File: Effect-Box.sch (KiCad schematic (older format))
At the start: 0 parts

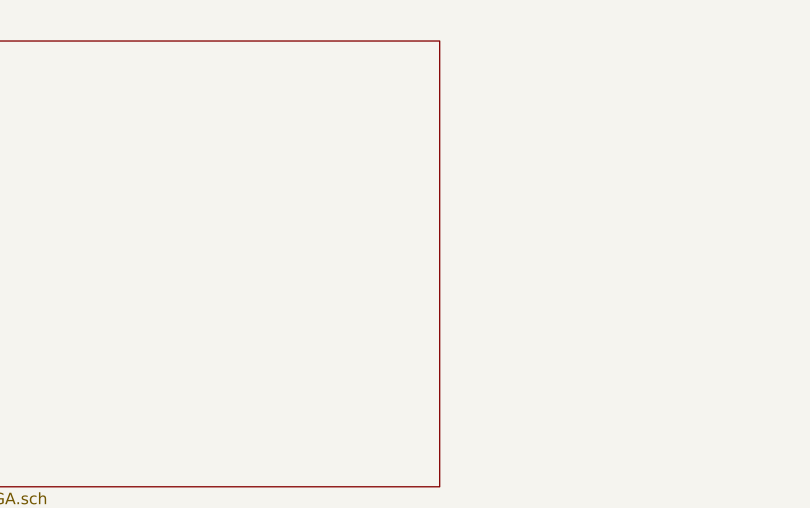
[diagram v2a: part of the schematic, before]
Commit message: Prepare FPGA I/O pins
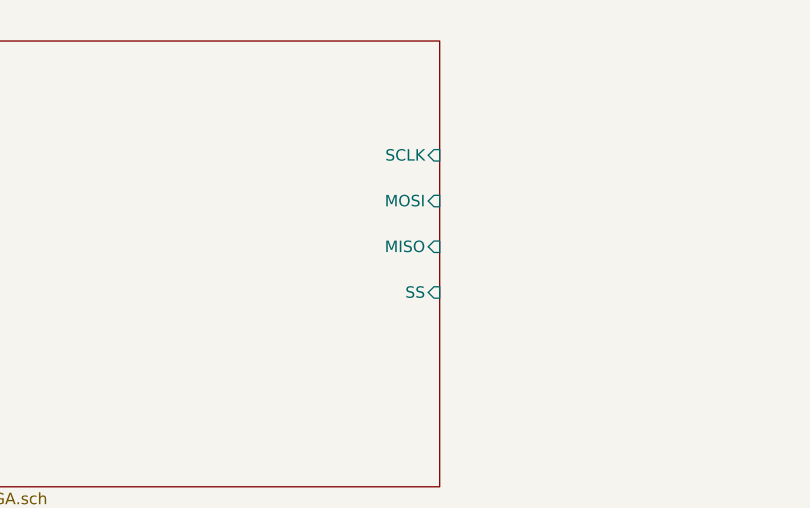
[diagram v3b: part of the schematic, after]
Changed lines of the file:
@@
 F0 "FPGA" 50
 F1 "FPGA.sch" 50
+F2 "SCLK" I R 3700 1900 50
+F3 "MOSI" I R 3700 2100 50
+F4 "MISO" I R 3700 2300 50
+F5 "SS" I R 3700 2500 50
 $EndSheet
 $Sheet

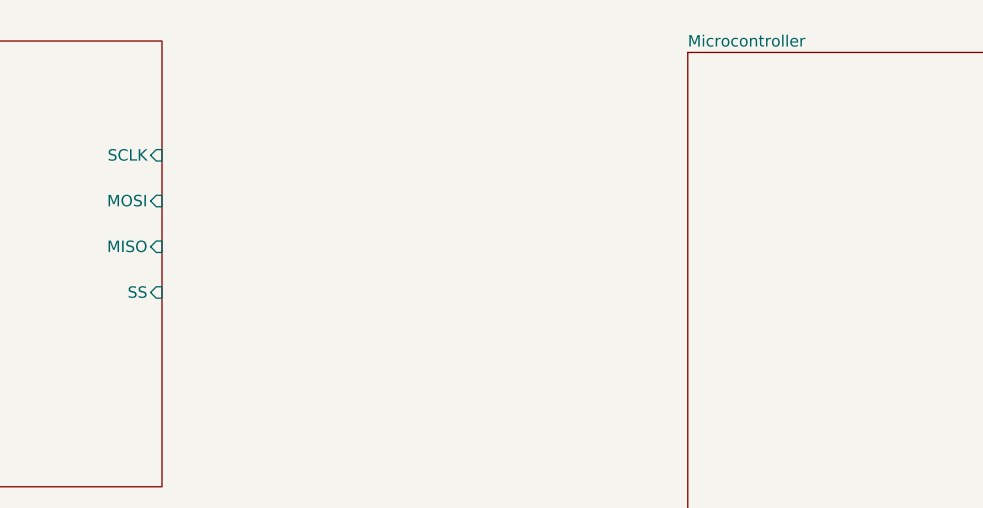
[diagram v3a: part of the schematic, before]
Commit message: Connect MCU to FPGA
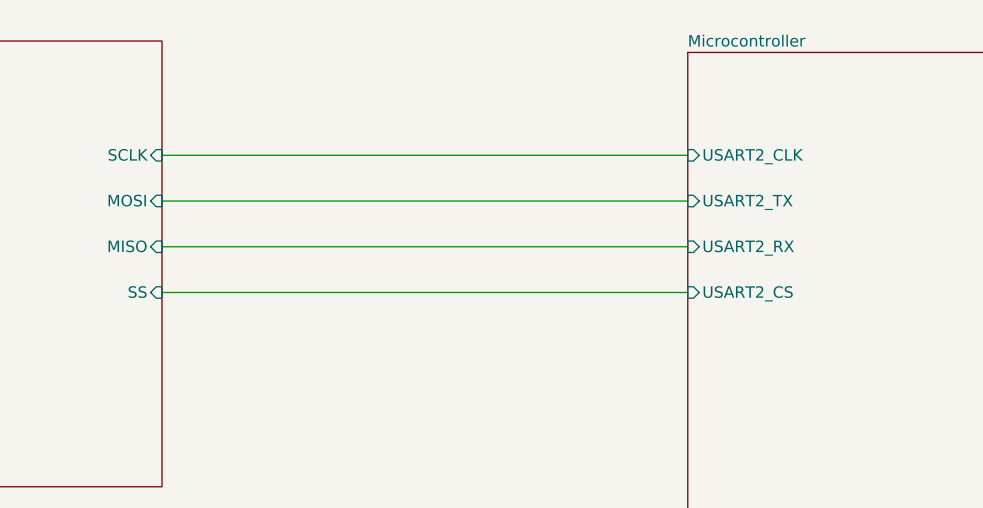
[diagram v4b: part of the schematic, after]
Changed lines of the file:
@@
 F0 "Microcontroller" 50
 F1 "microcontroller.sch" 50
+F2 "USART2_TX" I L 6000 2100 50
+F3 "USART2_RX" I L 6000 2300 50
+F4 "USART2_CLK" I L 6000 1900 50
+F5 "USART2_CS" I L 6000 2500 50
 $EndSheet
 $Sheet
@@
 F1 "power.sch" 50
 $EndSheet
+Wire Wire Line
+	6000 1900 3700 1900
+Wire Wire Line
+	6000 2100 3700 2100
+Wire Wire Line
+	6000 2300 3700 2300
+Wire Wire Line
+	6000 2500 3700 2500
 $EndSCHEMATC

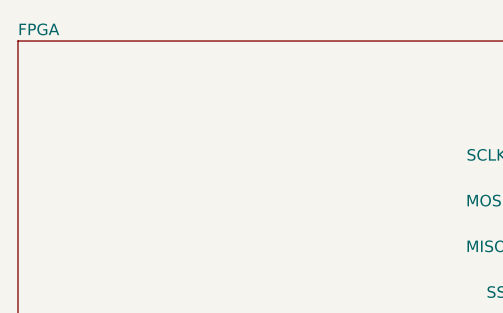
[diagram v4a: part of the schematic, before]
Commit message: Add NC symbols
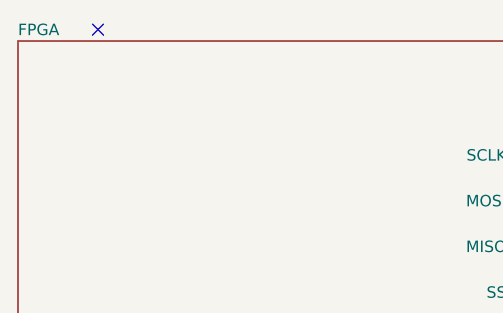
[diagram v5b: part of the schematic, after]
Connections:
- no-connect marks 0 -> 1
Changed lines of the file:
@@
 Wire Wire Line
 	6000 2500 3700 2500
+NoConn ~ 1850 1350
 $EndSCHEMATC

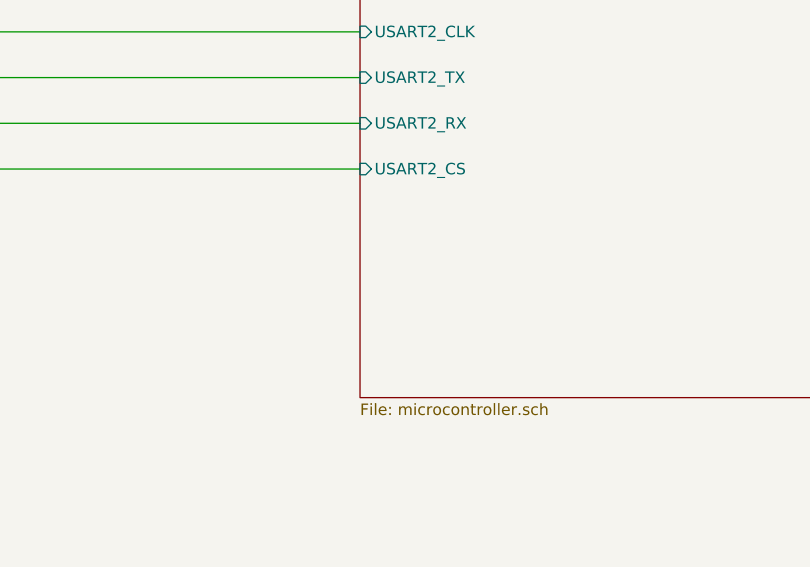
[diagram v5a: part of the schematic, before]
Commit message: Add 2x13 pin header
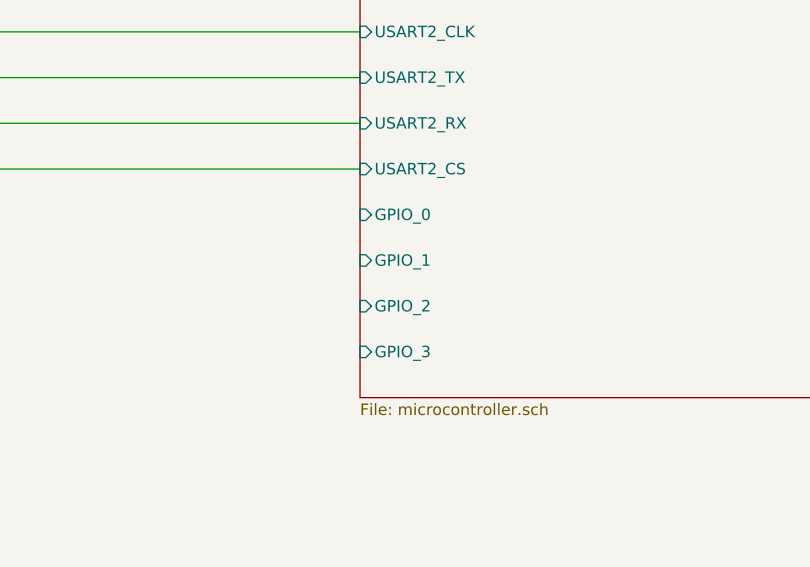
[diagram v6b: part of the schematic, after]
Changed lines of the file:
@@
-$EndSheet
-$Sheet
-S 6000 1450 3900 2050
-U 5D7D441F
-F0 "Microcontroller" 50
-F1 "microcontroller.sch" 50
-F2 "USART2_TX" I L 6000 2100 50
-F3 "USART2_RX" I L 6000 2300 50
-F4 "USART2_CLK" I L 6000 1900 50
-F5 "USART2_CS" I L 6000 2500 50
 $EndSheet
 $Sheet
@@
 	6000 2500 3700 2500
 NoConn ~ 1850 1350
+$Sheet
+S 6000 1450 3900 2050
+U 5D7D441F
+F0 "Microcontroller" 50
+F1 "microcontroller.sch" 50
+F2 "USART2_TX" I L 6000 2100 50
+F3 "USART2_RX" I L 6000 2300 50
+F4 "USART2_CLK" I L 6000 1900 50
+F5 "USART2_CS" I L 6000 2500 50
+F6 "GPIO_0" I L 6000 2700 50
+F7 "GPIO_1" I L 6000 2900 50
+F8 "GPIO_2" I L 6000 3100 50
+F9 "GPIO_3" I L 6000 3300 50
+$EndSheet
 $EndSCHEMATC

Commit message: FPGA cleanup
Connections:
- no-connect marks 1 -> 0
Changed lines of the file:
@@
 F0 "FPGA" 50
 F1 "FPGA.sch" 50
-F2 "SCLK" I R 3700 1900 50
-F3 "MOSI" I R 3700 2100 50
-F4 "MISO" I R 3700 2300 50
-F5 "SS" I R 3700 2500 50
+F2 "SCLK" I R 3700 1650 50
+F3 "MOSI" I R 3700 1850 50
+F4 "MISO" I R 3700 2050 50
+F5 "SS" I R 3700 2250 50
+F6 "GPIO_0" I R 3700 2450 50
+F7 "GPIO_1" I R 3700 2650 50
+F8 "GPIO_2" I R 3700 2850 50
+F9 "GPIO_3" I R 3700 3050 50
 $EndSheet
 $Sheet
@@
 $EndSheet
 Wire Wire Line
-	6000 1900 3700 1900
+	6000 1650 3700 1650
 Wire Wire Line
-	6000 2100 3700 2100
+	6000 1850 3700 1850
 Wire Wire Line
-	6000 2300 3700 2300
+	6000 2050 3700 2050
 Wire Wire Line
-	6000 2500 3700 2500
-NoConn ~ 1850 1350
+	6000 2250 3700 2250
 $Sheet
-S 6000 1450 3900 2050
+S 6000 1200 3900 2050
 U 5D7D441F
 F0 "Microcontroller" 50
 F1 "microcontroller.sch" 50
-F2 "USART2_TX" I L 6000 2100 50
-F3 "USART2_RX" I L 6000 2300 50
-F4 "USART2_CLK" I L 6000 1900 50
-F5 "USART2_CS" I L 6000 2500 50
-F6 "GPIO_0" I L 6000 2700 50
-F7 "GPIO_1" I L 6000 2900 50
-F8 "GPIO_2" I L 6000 3100 50
-F9 "GPIO_3" I L 6000 3300 50
+F2 "USART2_TX" I L 6000 1850 50
+F3 "USART2_RX" I L 6000 2050 50
+F4 "USART2_CLK" I L 6000 1650 50
+F5 "USART2_CS" I L 6000 2250 50
+F6 "GPIO_0" I L 6000 2450 50
+F7 "GPIO_1" I L 6000 2650 50
+F8 "GPIO_2" I L 6000 2850 50
+F9 "GPIO_3" I L 6000 3050 50
 $EndSheet
+Wire Wire Line
+	3700 2450 6000 2450
+Wire Wire Line
+	6000 2650 3700 2650
+Wire Wire Line
+	3700 2850 6000 2850
+Wire Wire Line
+	6000 3050 3700 3050
 $EndSCHEMATC

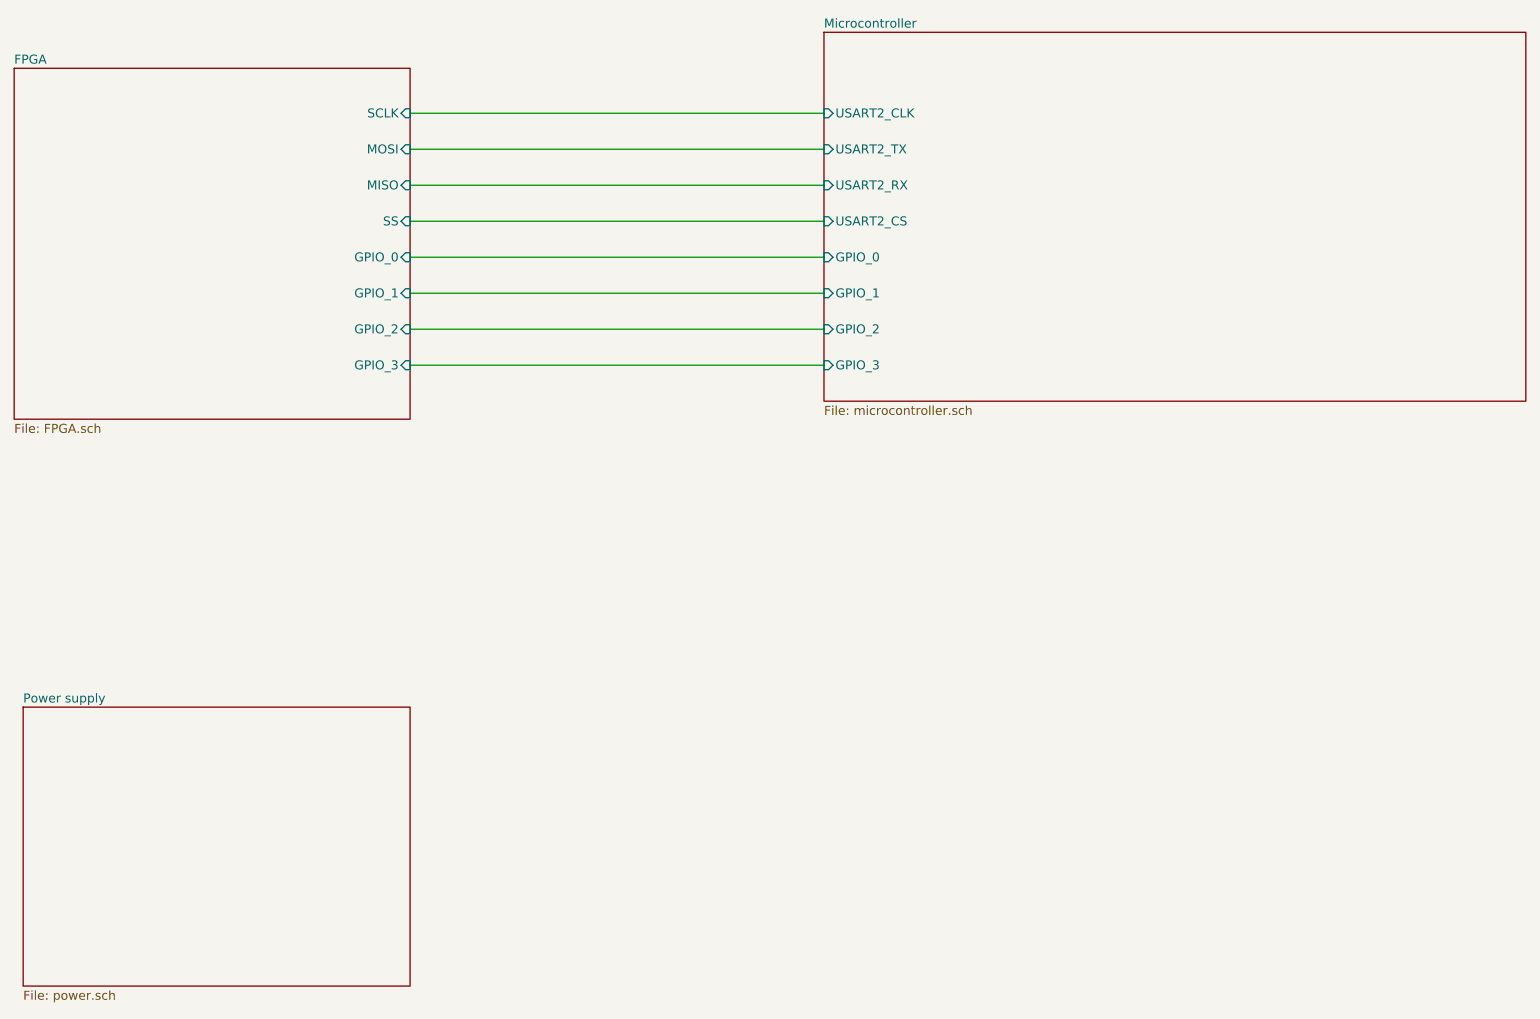
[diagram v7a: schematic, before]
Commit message: Minor FPGA and MCU fixes
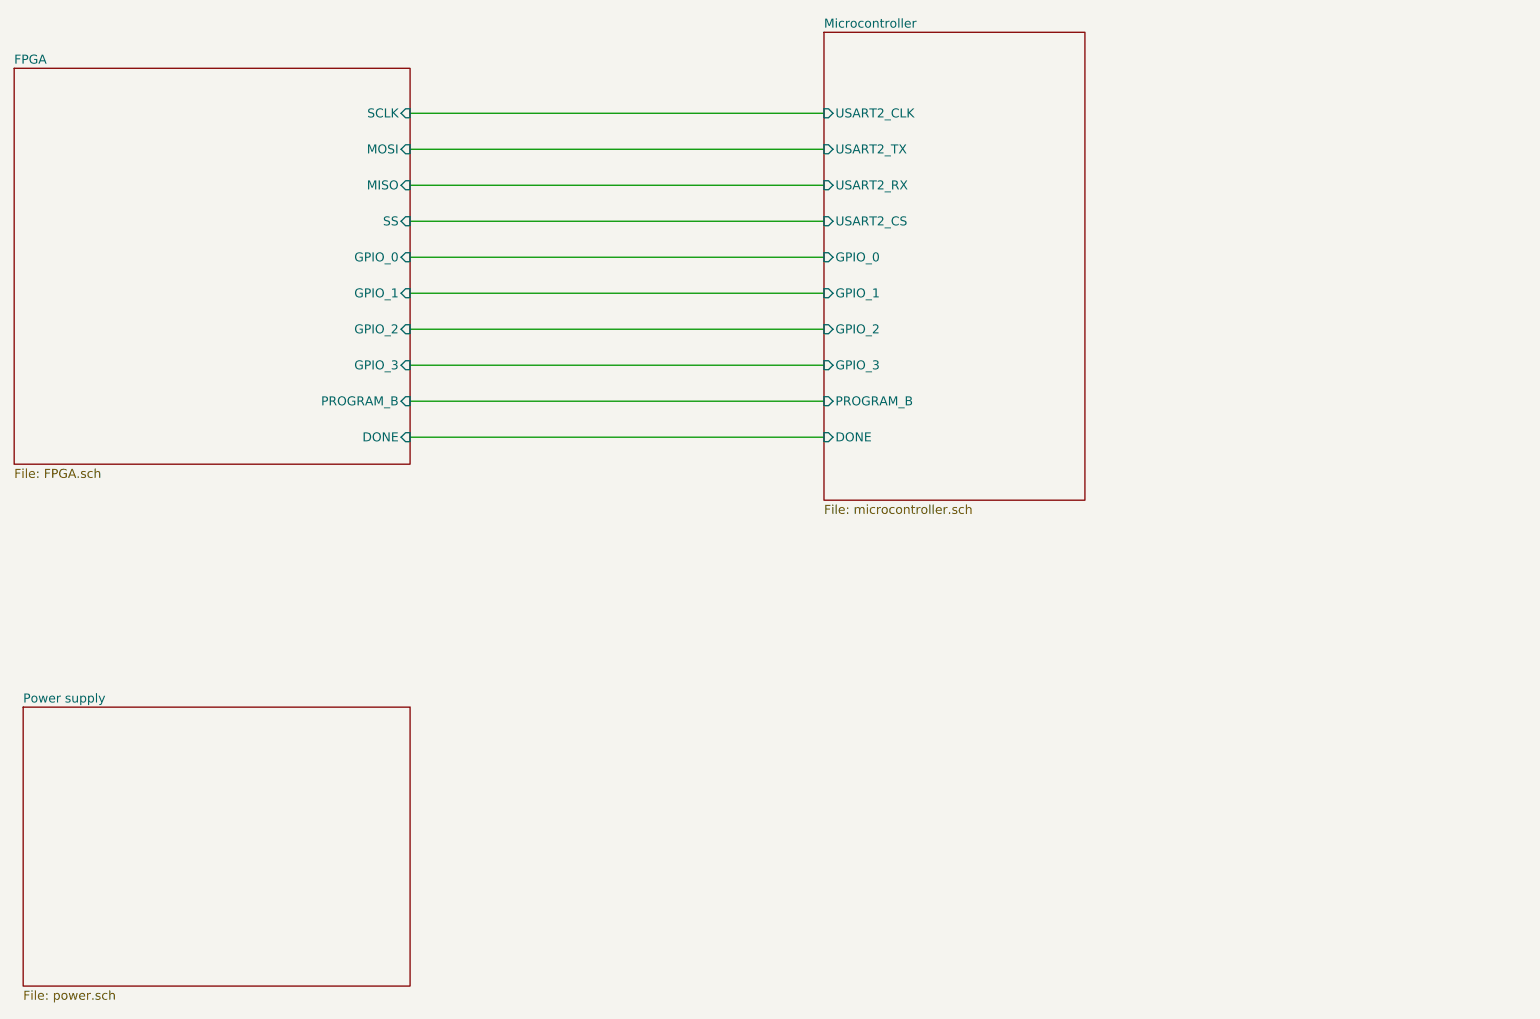
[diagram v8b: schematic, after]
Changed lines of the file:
@@
 $EndDescr
 $Sheet
-S 1500 1400 2200 1950
+S 1500 1400 2200 2200
 U 5D7D43D9
 F0 "FPGA" 50
@@
 F8 "GPIO_2" I R 3700 2850 50
 F9 "GPIO_3" I R 3700 3050 50
+F10 "PROGRAM_B" I R 3700 3250 50
+F11 "DONE" I R 3700 3450 50
 $EndSheet
 $Sheet
@@
 Wire Wire Line
 	6000 2250 3700 2250
+Wire Wire Line
+	3700 2450 6000 2450
+Wire Wire Line
+	6000 2650 3700 2650
+Wire Wire Line
+	3700 2850 6000 2850
+Wire Wire Line
+	6000 3050 3700 3050
 $Sheet
-S 6000 1200 3900 2050
+S 6000 1200 1450 2600
 U 5D7D441F
 F0 "Microcontroller" 50
@@
 F8 "GPIO_2" I L 6000 2850 50
 F9 "GPIO_3" I L 6000 3050 50
+F10 "PROGRAM_B" I L 6000 3250 50
+F11 "DONE" I L 6000 3450 50
 $EndSheet
 Wire Wire Line
-	3700 2450 6000 2450
+	3700 3250 6000 3250
 Wire Wire Line
-	6000 2650 3700 2650
-Wire Wire Line
-	3700 2850 6000 2850
-Wire Wire Line
-	6000 3050 3700 3050
+	6000 3450 3700 3450
 $EndSCHEMATC
